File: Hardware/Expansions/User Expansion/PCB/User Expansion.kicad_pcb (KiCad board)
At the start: 2 copper layers, 100 x 70 mm, 876 parts, among them J101 10018784-10201TLF, U101 M24C02-FMN

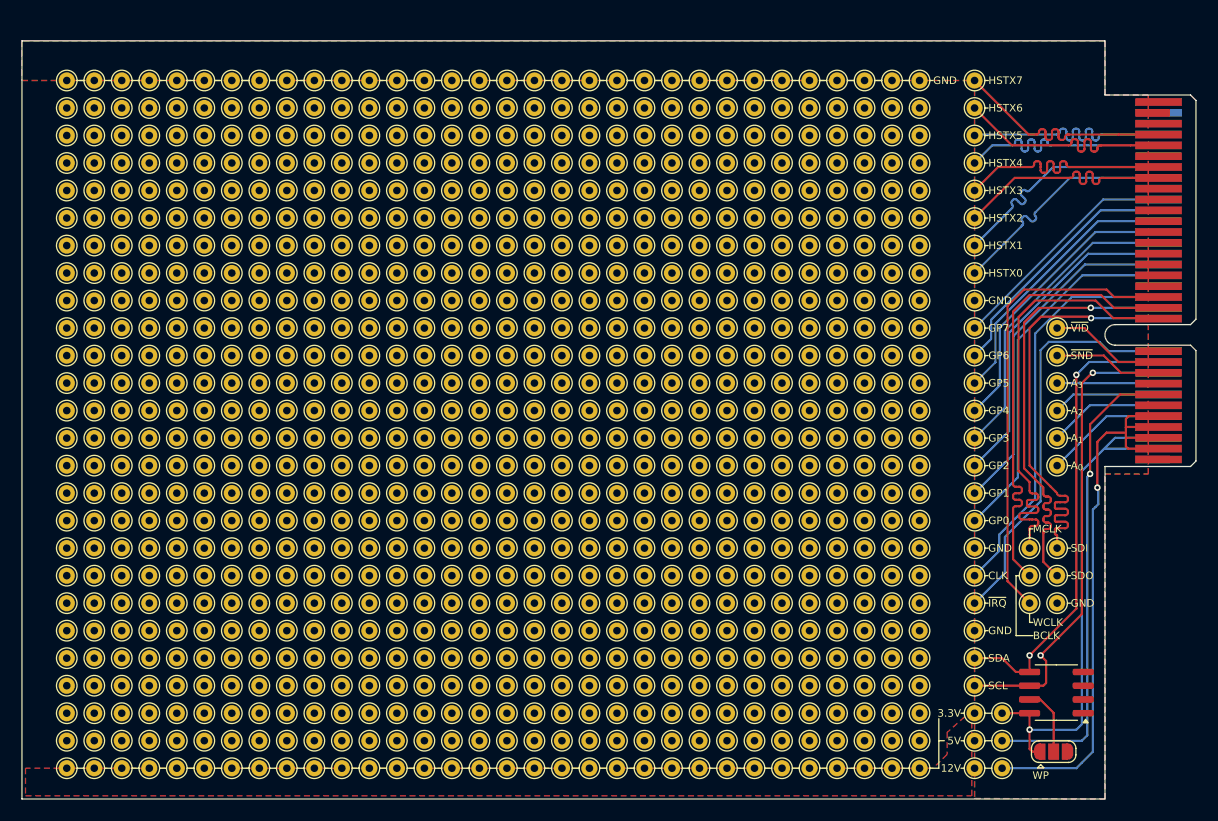
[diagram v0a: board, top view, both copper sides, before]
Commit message: Overhauls user expansion and updates design to new platform decisions.
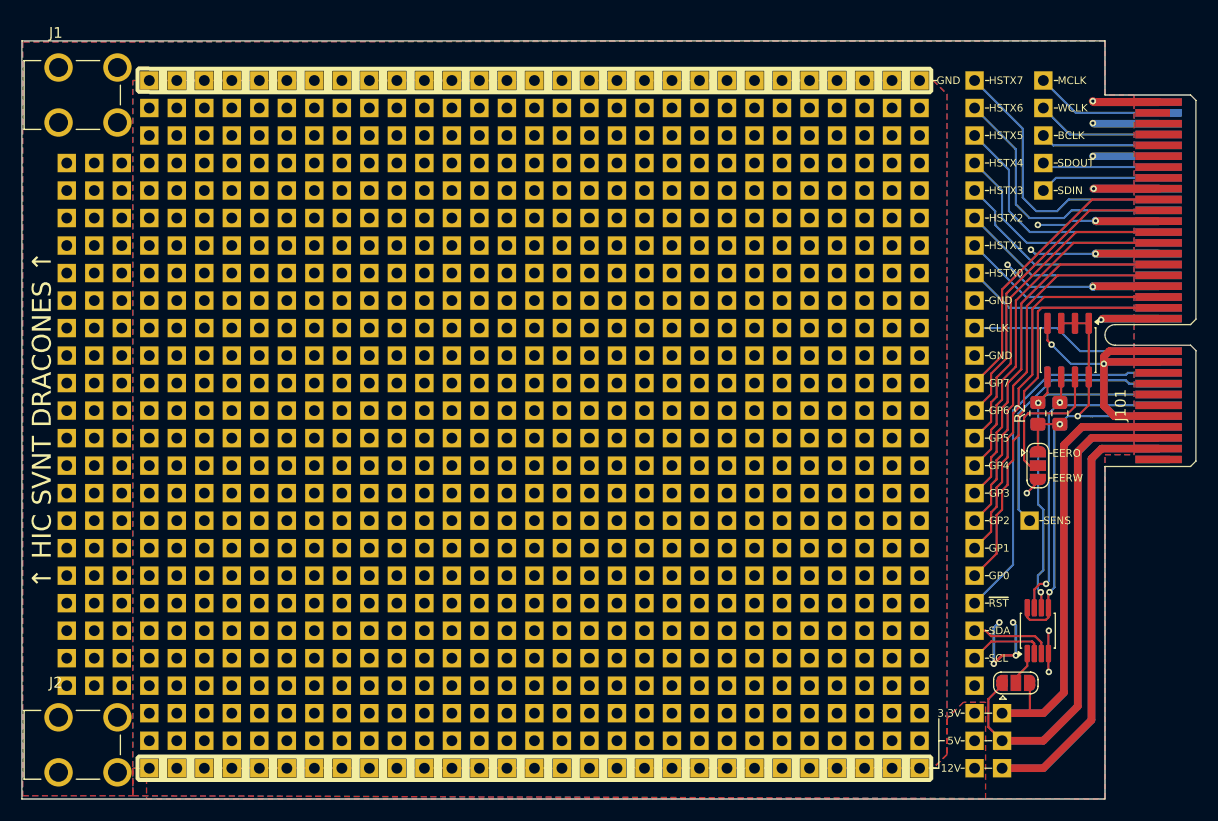
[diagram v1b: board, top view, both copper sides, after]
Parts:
- removed TP1001, TP1002, TP1003, TP1004, TP1005, TP1006, TP1007, TP1008, TP1009, TP1010, TP1011, TP1012, TP1013, TP1014, TP1015, TP1016, TP1017, TP1018, TP1019, TP1020, TP1021, TP1022, TP1023, TP1024, TP1025, TP1026, TP1027, TP1028, TP1029, TP1030, TP1031, TP1032, TP1033, TP1034, TP1035, TP1036, TP1037, TP1038, TP1039, TP1040, TP1041, TP1042, TP1043, TP1044, TP1045, TP1046, TP1047, TP1048, TP1049, TP1050, TP1051, TP1052, TP1053, TP1054, TP1055, TP1056, TP1057, TP1058, TP1059, TP1060, TP1061, TP1062, TP1063, TP1064, TP1101, TP1102, TP1103, TP1104, TP1105, TP1106, TP1107, TP1108, TP1109, TP1110, TP1111, TP1112, TP1113, TP1114, TP1115, TP1116, TP1117, TP1118, TP1119, TP1120, TP1121, TP1122, TP1123, TP1124, TP1125, TP1126, TP1127, TP1128, TP1129, TP1130, TP1131, TP1132, TP1133, TP1134, TP1135, TP1136, TP1137, TP1138, TP1139, TP1140, TP1141, TP1142, TP1143, TP1144, TP1145, TP1146, TP1147, TP1148, TP1149, TP1150, TP1151, TP1152, TP1153, TP1154, TP1155, TP1156, TP1157, TP1158, TP1159, TP1160, TP1161, TP1162, TP1163, TP1164, TP1201, TP1202, TP1203, TP1204, TP1205, TP1206, TP1207, TP1208, TP1209, TP1210, TP1211, TP1212, TP1213, TP1214, TP1215, TP1216, TP1217, TP1218, TP1219, TP1220, TP1221, TP1222, TP1223, TP1224, TP1225, TP1226, TP1227, TP1228, TP1229, TP1230, TP1231, TP1232, TP1233, TP1234, TP1235, TP1236, TP1237, TP1238, TP1239, TP1240, TP1241, TP1242, TP1243, TP1244, TP1245, TP1246, TP1247, TP1248, TP1249, TP1250, TP1251, TP1252, TP1253, TP1254, TP1255, TP1256, TP1257, TP1258, TP1259, TP1260, TP1261, TP1262, TP1263, TP1264, TP1330 (x2), TP1331 (x2), TP1332 (x2), TP1333, TP1334, TP1335, TP1336, TP1337, TP1338, TP1339, TP1340, TP1341, TP1342, TP1343, TP1344, TP1345, TP1346, TP1347, TP1348, TP1349, TP1350, TP1351, TP1352, TP1353, TP1354, TP1355, TP1356, TP1357, TP1358, TP1359, TP1360, TP1361, TP1362, TP1363, TP1364, TP1424, TP1428, TP1432, TP201, TP202, TP203, TP204, TP205, TP206, TP207, TP208, TP209, TP210, TP211, TP212, TP213, TP214, TP215, TP216, TP217, TP218, TP219, TP220, TP221, TP222, TP223, TP224, TP225, TP226, TP227, TP228, TP229, TP230, TP231, TP232, TP233, TP234, TP235, TP236, TP237, TP238, TP239, TP240, TP241, TP242, TP243, TP244, TP245, TP246, TP247, TP248, TP249, TP250, TP251, TP252, TP253, TP254, TP255, TP256, TP257, TP258, TP259, TP260, TP261, TP262, TP263, TP264, TP301, TP302, TP303, TP304, TP305, TP306, TP307, TP308, TP309, TP310, TP311, TP312, TP313, TP314, TP315, TP316, TP317, TP318, TP319, TP320, TP321, TP322, TP323, TP324, TP325, TP326, TP327, TP328, TP329, TP330, TP331, TP332, TP333, TP334, TP335, TP336, TP337, TP338, TP339, TP340, TP341, TP342, TP343, TP344, TP345, TP346, TP347, TP348, TP349, TP350, TP351, TP352, TP353, TP354, TP355, TP356, TP357, TP358, TP359, TP360, TP361, TP362, TP363, TP364, TP401, TP402, TP403, TP404, TP405, TP406, TP407, TP408, TP409, TP410, TP411, TP412, TP413, TP414, TP415, TP416, TP417, TP418, TP419, TP420, TP421, TP422, TP423, TP424, TP425, TP426, TP427, TP428, TP429, TP430, TP431, TP432, TP433, TP434, TP435, TP436, TP437, TP438, TP439, TP440, TP441, TP442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: -, TestPoint:TestPoint_THTPad_D1.5mm_Drill0.7mm
- removed TP102: SCL, TestPoint:TestPoint_THTPad_D1.5mm_Drill0.7mm
- removed TP103: SDA, TestPoint:TestPoint_THTPad_D1.5mm_Drill0.7mm
- removed TP128: WCLK, TestPoint:TestPoint_THTPad_D1.5mm_Drill0.7mm
- removed TP129: HSTX2, TestPoint:TestPoint_THTPad_D1.5mm_Drill0.7mm
- removed TP130: HSTX3, TestPoint:TestPoint_THTPad_D1.5mm_Drill0.7mm
- removed the TP1301 at (165.1, 96.5)
- removed the TP1302 at (165.1, 104.1)
- removed the TP1303 at (167.6, 94.0)
- removed the TP1304 at (167.6, 104.1)
- removed the TP1305 at (175.3, 94.0)
- removed the TP1306 at (175.3, 96.5)
- removed the TP1307 at (175.3, 99.1)
- removed the TP1308 at (175.3, 101.6)
- removed the TP1309 at (165.1, 94.0)
- removed TP131: HSTX6, TestPoint:TestPoint_THTPad_D1.5mm_Drill0.7mm
- removed the TP1310 at (165.1, 106.7)
- removed the TP1311 at (167.6, 96.5)
- removed the TP1312 at (167.6, 106.7)
- removed the TP1313 at (175.3, 104.1)
- removed the TP1314 at (175.3, 106.7)
- removed the TP1315 at (175.3, 109.2)
- removed the TP1316 at (175.3, 111.8)
- removed the TP1317 at (165.1, 99.1)
- removed the TP1318 at (165.1, 109.2)
- removed the TP1319 at (167.6, 99.1)
- removed the TP1320 at (167.6, 109.2)
- removed the TP1321 at (177.8, 94.0)
- removed the TP1322 at (177.8, 96.5)
- removed the TP1323 at (177.8, 99.1)
- removed the TP1324 at (177.8, 101.6)
- removed the TP1325 at (165.1, 101.6)
- removed the TP1326 at (165.1, 111.8)
- removed the TP1327 at (167.6, 101.6)
- removed the TP1328 at (167.6, 111.8)
- removed the TP1329 at (177.8, 104.1)
- removed TP134: GP7, TestPoint:TestPoint_THTPad_D1.5mm_Drill0.7mm
- removed U101: M24C02-FMN, Package_SO:SOIC-8_3.9x4.9mm_P1.27mm
- added J1: 7774, Home Computer:KEYSTONE_7774, F.Cu at (106.1, 75.0)
- added J2: 7774, Home Computer:KEYSTONE_7774, F.Cu at (106.1, 135.0)
- added JP102: WP, Jumper:SolderJumper-3_P1.3mm_Open_RoundedPad1.0x1.5mm, F.Cu at (191.8, 129.3)
- added R1: 10K, Resistor_SMD:R_0805_2012Metric_Pad1.20x1.40mm_HandSolder, F.Cu at (195.8, 104.4)
- added R2: 10K, Resistor_SMD:R_0805_2012Metric_Pad1.20x1.40mm_HandSolder, F.Cu at (193.8, 104.4)
- added REF**10: Home Computer:Perfboard_Pad_P2.54mm, Home Computer:Perfboard_Pad_P2.54mm, F.Cu at (129.5, 76.2)
- added REF**100: Home Computer:Perfboard_Pad_P2.54mm, Home Computer:Perfboard_Pad_P2.54mm, F.Cu at (114.3, 83.8)
- added REF**101: Home Computer:Perfboard_Pad_P2.54mm, Home Computer:Perfboard_Pad_P2.54mm, F.Cu at (116.8, 83.8)
- added REF**102: Home Computer:Perfboard_Pad_P2.54mm, Home Computer:Perfboard_Pad_P2.54mm, F.Cu at (119.4, 83.8)
- added REF**103: Home Computer:Perfboard_Pad_P2.54mm, Home Computer:Perfboard_Pad_P2.54mm, F.Cu at (121.9, 83.8)
- added REF**104: Home Computer:Perfboard_Pad_P2.54mm, Home Computer:Perfboard_Pad_P2.54mm, F.Cu at (124.5, 83.8)
- added REF**105: Home Computer:Perfboard_Pad_P2.54mm, Home Computer:Perfboard_Pad_P2.54mm, F.Cu at (127.0, 83.8)
- added REF**106: Home Computer:Perfboard_Pad_P2.54mm, Home Computer:Perfboard_Pad_P2.54mm, F.Cu at (129.5, 83.8)
- added REF**107: Home Computer:Perfboard_Pad_P2.54mm, Home Computer:Perfboard_Pad_P2.54mm, F.Cu at (132.1, 83.8)
- added REF**108: Home Computer:Perfboard_Pad_P2.54mm, Home Computer:Perfboard_Pad_P2.54mm, F.Cu at (134.6, 83.8)
- added REF**109: Home Computer:Perfboard_Pad_P2.54mm, Home Computer:Perfboard_Pad_P2.54mm, F.Cu at (137.2, 83.8)
- added REF**11: Home Computer:Perfboard_Pad_P2.54mm, Home Computer:Perfboard_Pad_P2.54mm, F.Cu at (132.1, 76.2)
- added REF**110: Home Computer:Perfboard_Pad_P2.54mm, Home Computer:Perfboard_Pad_P2.54mm, F.Cu at (139.7, 83.8)
- added REF**111: Home Computer:Perfboard_Pad_P2.54mm, Home Computer:Perfboard_Pad_P2.54mm, F.Cu at (142.2, 83.8)
- added REF**112: Home Computer:Perfboard_Pad_P2.54mm, Home Computer:Perfboard_Pad_P2.54mm, F.Cu at (144.8, 83.8)
- added REF**113: Home Computer:Perfboard_Pad_P2.54mm, Home Computer:Perfboard_Pad_P2.54mm, F.Cu at (147.3, 83.8)
- added REF**114: Home Computer:Perfboard_Pad_P2.54mm, Home Computer:Perfboard_Pad_P2.54mm, F.Cu at (149.9, 83.8)
- added REF**115: Home Computer:Perfboard_Pad_P2.54mm, Home Computer:Perfboard_Pad_P2.54mm, F.Cu at (152.4, 83.8)
- added REF**116: Home Computer:Perfboard_Pad_P2.54mm, Home Computer:Perfboard_Pad_P2.54mm, F.Cu at (154.9, 83.8)
- added REF**117: Home Computer:Perfboard_Pad_P2.54mm, Home Computer:Perfboard_Pad_P2.54mm, F.Cu at (157.5, 83.8)
- added REF**118: Home Computer:Perfboard_Pad_P2.54mm, Home Computer:Perfboard_Pad_P2.54mm, F.Cu at (160.0, 83.8)
- added REF**119: Home Computer:Perfboard_Pad_P2.54mm, Home Computer:Perfboard_Pad_P2.54mm, F.Cu at (162.6, 83.8)
- added REF**12: Home Computer:Perfboard_Pad_P2.54mm, Home Computer:Perfboard_Pad_P2.54mm, F.Cu at (134.6, 76.2)
- added REF**120: Home Computer:Perfboard_Pad_P2.54mm, Home Computer:Perfboard_Pad_P2.54mm, F.Cu at (165.1, 83.8)
- added REF**121: Home Computer:Perfboard_Pad_P2.54mm, Home Computer:Perfboard_Pad_P2.54mm, F.Cu at (167.6, 83.8)
- added REF**122: Home Computer:Perfboard_Pad_P2.54mm, Home Computer:Perfboard_Pad_P2.54mm, F.Cu at (170.2, 83.8)
- added REF**123: Home Computer:Perfboard_Pad_P2.54mm, Home Computer:Perfboard_Pad_P2.54mm, F.Cu at (172.7, 83.8)
- added REF**124: Home Computer:Perfboard_Pad_P2.54mm, Home Computer:Perfboard_Pad_P2.54mm, F.Cu at (175.3, 83.8)
- added REF**125: Home Computer:Perfboard_Pad_P2.54mm, Home Computer:Perfboard_Pad_P2.54mm, F.Cu at (177.8, 83.8)
- added REF**126: Home Computer:Perfboard_Pad_P2.54mm, Home Computer:Perfboard_Pad_P2.54mm, F.Cu at (180.3, 83.8)
- added REF**127: Home Computer:Perfboard_Pad_P2.54mm, Home Computer:Perfboard_Pad_P2.54mm, F.Cu at (182.9, 83.8)
- added REF**128: Home Computer:Perfboard_Pad_P2.54mm, Home Computer:Perfboard_Pad_P2.54mm, F.Cu at (104.1, 86.4)
- added REF**129: Home Computer:Perfboard_Pad_P2.54mm, Home Computer:Perfboard_Pad_P2.54mm, F.Cu at (106.7, 86.4)
- added REF**13: Home Computer:Perfboard_Pad_P2.54mm, Home Computer:Perfboard_Pad_P2.54mm, F.Cu at (137.2, 76.2)
- added REF**130: Home Computer:Perfboard_Pad_P2.54mm, Home Computer:Perfboard_Pad_P2.54mm, F.Cu at (109.2, 86.4)
- added REF**131: Home Computer:Perfboard_Pad_P2.54mm, Home Computer:Perfboard_Pad_P2.54mm, F.Cu at (111.8, 86.4)
- added REF**132: Home Computer:Perfboard_Pad_P2.54mm, Home Computer:Perfboard_Pad_P2.54mm, F.Cu at (114.3, 86.4)
- added REF**133: Home Computer:Perfboard_Pad_P2.54mm, Home Computer:Perfboard_Pad_P2.54mm, F.Cu at (116.8, 86.4)
- added REF**134: Home Computer:Perfboard_Pad_P2.54mm, Home Computer:Perfboard_Pad_P2.54mm, F.Cu at (119.4, 86.4)
- added REF**135: Home Computer:Perfboard_Pad_P2.54mm, Home Computer:Perfboard_Pad_P2.54mm, F.Cu at (121.9, 86.4)
- added REF**136: Home Computer:Perfboard_Pad_P2.54mm, Home Computer:Perfboard_Pad_P2.54mm, F.Cu at (124.5, 86.4)
- added REF**137: Home Computer:Perfboard_Pad_P2.54mm, Home Computer:Perfboard_Pad_P2.54mm, F.Cu at (127.0, 86.4)
- added REF**138: Home Computer:Perfboard_Pad_P2.54mm, Home Computer:Perfboard_Pad_P2.54mm, F.Cu at (129.5, 86.4)
- added REF**139: Home Computer:Perfboard_Pad_P2.54mm, Home Computer:Perfboard_Pad_P2.54mm, F.Cu at (132.1, 86.4)
- added REF**14: Home Computer:Perfboard_Pad_P2.54mm, Home Computer:Perfboard_Pad_P2.54mm, F.Cu at (139.7, 76.2)
- added REF**140: Home Computer:Perfboard_Pad_P2.54mm, Home Computer:Perfboard_Pad_P2.54mm, F.Cu at (134.6, 86.4)
- added REF**141: Home Computer:Perfboard_Pad_P2.54mm, Home Computer:Perfboard_Pad_P2.54mm, F.Cu at (137.2, 86.4)
- added REF**142: Home Computer:Perfboard_Pad_P2.54mm, Home Computer:Perfboard_Pad_P2.54mm, F.Cu at (139.7, 86.4)
- added REF**143: Home Computer:Perfboard_Pad_P2.54mm, Home Computer:Perfboard_Pad_P2.54mm, F.Cu at (142.2, 86.4)
- added REF**144: Home Computer:Perfboard_Pad_P2.54mm, Home Computer:Perfboard_Pad_P2.54mm, F.Cu at (144.8, 86.4)
- added REF**145: Home Computer:Perfboard_Pad_P2.54mm, Home Computer:Perfboard_Pad_P2.54mm, F.Cu at (147.3, 86.4)
- added REF**146: Home Computer:Perfboard_Pad_P2.54mm, Home Computer:Perfboard_Pad_P2.54mm, F.Cu at (149.9, 86.4)
- added REF**147: Home Computer:Perfboard_Pad_P2.54mm, Home Computer:Perfboard_Pad_P2.54mm, F.Cu at (152.4, 86.4)
- added REF**148: Home Computer:Perfboard_Pad_P2.54mm, Home Computer:Perfboard_Pad_P2.54mm, F.Cu at (154.9, 86.4)
- added REF**149: Home Computer:Perfboard_Pad_P2.54mm, Home Computer:Perfboard_Pad_P2.54mm, F.Cu at (157.5, 86.4)
- added REF**15: Home Computer:Perfboard_Pad_P2.54mm, Home Computer:Perfboard_Pad_P2.54mm, F.Cu at (142.2, 76.2)
- added REF**150: Home Computer:Perfboard_Pad_P2.54mm, Home Computer:Perfboard_Pad_P2.54mm, F.Cu at (160.0, 86.4)
- added REF**151: Home Computer:Perfboard_Pad_P2.54mm, Home Computer:Perfboard_Pad_P2.54mm, F.Cu at (162.6, 86.4)
- added REF**152: Home Computer:Perfboard_Pad_P2.54mm, Home Computer:Perfboard_Pad_P2.54mm, F.Cu at (165.1, 86.4)
- added REF**153: Home Computer:Perfboard_Pad_P2.54mm, Home Computer:Perfboard_Pad_P2.54mm, F.Cu at (167.6, 86.4)
- added REF**154: Home Computer:Perfboard_Pad_P2.54mm, Home Computer:Perfboard_Pad_P2.54mm, F.Cu at (170.2, 86.4)
- added REF**155: Home Computer:Perfboard_Pad_P2.54mm, Home Computer:Perfboard_Pad_P2.54mm, F.Cu at (172.7, 86.4)
- added REF**156: Home Computer:Perfboard_Pad_P2.54mm, Home Computer:Perfboard_Pad_P2.54mm, F.Cu at (175.3, 86.4)
- added REF**157: Home Computer:Perfboard_Pad_P2.54mm, Home Computer:Perfboard_Pad_P2.54mm, F.Cu at (177.8, 86.4)
- added REF**158: Home Computer:Perfboard_Pad_P2.54mm, Home Computer:Perfboard_Pad_P2.54mm, F.Cu at (180.3, 86.4)
- added REF**159: Home Computer:Perfboard_Pad_P2.54mm, Home Computer:Perfboard_Pad_P2.54mm, F.Cu at (182.9, 86.4)
- added REF**16: Home Computer:Perfboard_Pad_P2.54mm, Home Computer:Perfboard_Pad_P2.54mm, F.Cu at (144.8, 76.2)
- added REF**160: Home Computer:Perfboard_Pad_P2.54mm, Home Computer:Perfboard_Pad_P2.54mm, F.Cu at (104.1, 88.9)
- added REF**161: Home Computer:Perfboard_Pad_P2.54mm, Home Computer:Perfboard_Pad_P2.54mm, F.Cu at (106.7, 88.9)
- added REF**162: Home Computer:Perfboard_Pad_P2.54mm, Home Computer:Perfboard_Pad_P2.54mm, F.Cu at (109.2, 88.9)
- added REF**163: Home Computer:Perfboard_Pad_P2.54mm, Home Computer:Perfboard_Pad_P2.54mm, F.Cu at (111.8, 88.9)
- added REF**164: Home Computer:Perfboard_Pad_P2.54mm, Home Computer:Perfboard_Pad_P2.54mm, F.Cu at (114.3, 88.9)
- added REF**165: Home Computer:Perfboard_Pad_P2.54mm, Home Computer:Perfboard_Pad_P2.54mm, F.Cu at (116.8, 88.9)
- added REF**166: Home Computer:Perfboard_Pad_P2.54mm, Home Computer:Perfboard_Pad_P2.54mm, F.Cu at (119.4, 88.9)
- added REF**167: Home Computer:Perfboard_Pad_P2.54mm, Home Computer:Perfboard_Pad_P2.54mm, F.Cu at (121.9, 88.9)
- added REF**168: Home Computer:Perfboard_Pad_P2.54mm, Home Computer:Perfboard_Pad_P2.54mm, F.Cu at (124.5, 88.9)
- added REF**169: Home Computer:Perfboard_Pad_P2.54mm, Home Computer:Perfboard_Pad_P2.54mm, F.Cu at (127.0, 88.9)
- added REF**17: Home Computer:Perfboard_Pad_P2.54mm, Home Computer:Perfboard_Pad_P2.54mm, F.Cu at (147.3, 76.2)
- added REF**170: Home Computer:Perfboard_Pad_P2.54mm, Home Computer:Perfboard_Pad_P2.54mm, F.Cu at (129.5, 88.9)
- added REF**171: Home Computer:Perfboard_Pad_P2.54mm, Home Computer:Perfboard_Pad_P2.54mm, F.Cu at (132.1, 88.9)
- added REF**172: Home Computer:Perfboard_Pad_P2.54mm, Home Computer:Perfboard_Pad_P2.54mm, F.Cu at (134.6, 88.9)
- added REF**173: Home Computer:Perfboard_Pad_P2.54mm, Home Computer:Perfboard_Pad_P2.54mm, F.Cu at (137.2, 88.9)
- added REF**174: Home Computer:Perfboard_Pad_P2.54mm, Home Computer:Perfboard_Pad_P2.54mm, F.Cu at (139.7, 88.9)
- added REF**175: Home Computer:Perfboard_Pad_P2.54mm, Home Computer:Perfboard_Pad_P2.54mm, F.Cu at (142.2, 88.9)
- added REF**176: Home Computer:Perfboard_Pad_P2.54mm, Home Computer:Perfboard_Pad_P2.54mm, F.Cu at (144.8, 88.9)
- added REF**177: Home Computer:Perfboard_Pad_P2.54mm, Home Computer:Perfboard_Pad_P2.54mm, F.Cu at (147.3, 88.9)
- added REF**178: Home Computer:Perfboard_Pad_P2.54mm, Home Computer:Perfboard_Pad_P2.54mm, F.Cu at (149.9, 88.9)
- added REF**179: Home Computer:Perfboard_Pad_P2.54mm, Home Computer:Perfboard_Pad_P2.54mm, F.Cu at (152.4, 88.9)
- added REF**18: Home Computer:Perfboard_Pad_P2.54mm, Home Computer:Perfboard_Pad_P2.54mm, F.Cu at (149.9, 76.2)
- added REF**180: Home Computer:Perfboard_Pad_P2.54mm, Home Computer:Perfboard_Pad_P2.54mm, F.Cu at (154.9, 88.9)
- added REF**181: Home Computer:Perfboard_Pad_P2.54mm, Home Computer:Perfboard_Pad_P2.54mm, F.Cu at (157.5, 88.9)
- added REF**182: Home Computer:Perfboard_Pad_P2.54mm, Home Computer:Perfboard_Pad_P2.54mm, F.Cu at (160.0, 88.9)
- added REF**183: Home Computer:Perfboard_Pad_P2.54mm, Home Computer:Perfboard_Pad_P2.54mm, F.Cu at (162.6, 88.9)
- added REF**184: Home Computer:Perfboard_Pad_P2.54mm, Home Computer:Perfboard_Pad_P2.54mm, F.Cu at (165.1, 88.9)
- added REF**185: Home Computer:Perfboard_Pad_P2.54mm, Home Computer:Perfboard_Pad_P2.54mm, F.Cu at (167.6, 88.9)
- added REF**186: Home Computer:Perfboard_Pad_P2.54mm, Home Computer:Perfboard_Pad_P2.54mm, F.Cu at (170.2, 88.9)
- added REF**187: Home Computer:Perfboard_Pad_P2.54mm, Home Computer:Perfboard_Pad_P2.54mm, F.Cu at (172.7, 88.9)
- added REF**188: Home Computer:Perfboard_Pad_P2.54mm, Home Computer:Perfboard_Pad_P2.54mm, F.Cu at (175.3, 88.9)
- added REF**189: Home Computer:Perfboard_Pad_P2.54mm, Home Computer:Perfboard_Pad_P2.54mm, F.Cu at (177.8, 88.9)
- added REF**19: Home Computer:Perfboard_Pad_P2.54mm, Home Computer:Perfboard_Pad_P2.54mm, F.Cu at (152.4, 76.2)
- added REF**190: Home Computer:Perfboard_Pad_P2.54mm, Home Computer:Perfboard_Pad_P2.54mm, F.Cu at (180.3, 88.9)
- added REF**191: Home Computer:Perfboard_Pad_P2.54mm, Home Computer:Perfboard_Pad_P2.54mm, F.Cu at (182.9, 88.9)
- added REF**192: Home Computer:Perfboard_Pad_P2.54mm, Home Computer:Perfboard_Pad_P2.54mm, F.Cu at (104.1, 91.4)
- added REF**193: Home Computer:Perfboard_Pad_P2.54mm, Home Computer:Perfboard_Pad_P2.54mm, F.Cu at (106.7, 91.4)
- added REF**194: Home Computer:Perfboard_Pad_P2.54mm, Home Computer:Perfboard_Pad_P2.54mm, F.Cu at (109.2, 91.4)
- added REF**195: Home Computer:Perfboard_Pad_P2.54mm, Home Computer:Perfboard_Pad_P2.54mm, F.Cu at (111.8, 91.4)
- added REF**196: Home Computer:Perfboard_Pad_P2.54mm, Home Computer:Perfboard_Pad_P2.54mm, F.Cu at (114.3, 91.4)
- added REF**197: Home Computer:Perfboard_Pad_P2.54mm, Home Computer:Perfboard_Pad_P2.54mm, F.Cu at (116.8, 91.4)
- added REF**198: Home Computer:Perfboard_Pad_P2.54mm, Home Computer:Perfboard_Pad_P2.54mm, F.Cu at (119.4, 91.4)
- added REF**199: Home Computer:Perfboard_Pad_P2.54mm, Home Computer:Perfboard_Pad_P2.54mm, F.Cu at (121.9, 91.4)
- added REF**20: Home Computer:Perfboard_Pad_P2.54mm, Home Computer:Perfboard_Pad_P2.54mm, F.Cu at (154.9, 76.2)
- added REF**200: Home Computer:Perfboard_Pad_P2.54mm, Home Computer:Perfboard_Pad_P2.54mm, F.Cu at (124.5, 91.4)
- added REF**201: Home Computer:Perfboard_Pad_P2.54mm, Home Computer:Perfboard_Pad_P2.54mm, F.Cu at (127.0, 91.4)
- added REF**202: Home Computer:Perfboard_Pad_P2.54mm, Home Computer:Perfboard_Pad_P2.54mm, F.Cu at (129.5, 91.4)
- added REF**203: Home Computer:Perfboard_Pad_P2.54mm, Home Computer:Perfboard_Pad_P2.54mm, F.Cu at (132.1, 91.4)
- added REF**204: Home Computer:Perfboard_Pad_P2.54mm, Home Computer:Perfboard_Pad_P2.54mm, F.Cu at (134.6, 91.4)
- added REF**205: Home Computer:Perfboard_Pad_P2.54mm, Home Computer:Perfboard_Pad_P2.54mm, F.Cu at (137.2, 91.4)
- added REF**206: Home Computer:Perfboard_Pad_P2.54mm, Home Computer:Perfboard_Pad_P2.54mm, F.Cu at (139.7, 91.4)
- added REF**207: Home Computer:Perfboard_Pad_P2.54mm, Home Computer:Perfboard_Pad_P2.54mm, F.Cu at (142.2, 91.4)
- added REF**208: Home Computer:Perfboard_Pad_P2.54mm, Home Computer:Perfboard_Pad_P2.54mm, F.Cu at (144.8, 91.4)
- added REF**209: Home Computer:Perfboard_Pad_P2.54mm, Home Computer:Perfboard_Pad_P2.54mm, F.Cu at (147.3, 91.4)
- added REF**21: Home Computer:Perfboard_Pad_P2.54mm, Home Computer:Perfboard_Pad_P2.54mm, F.Cu at (157.5, 76.2)
- added REF**210: Home Computer:Perfboard_Pad_P2.54mm, Home Computer:Perfboard_Pad_P2.54mm, F.Cu at (149.9, 91.4)
- added REF**211: Home Computer:Perfboard_Pad_P2.54mm, Home Computer:Perfboard_Pad_P2.54mm, F.Cu at (152.4, 91.4)
- added REF**212: Home Computer:Perfboard_Pad_P2.54mm, Home Computer:Perfboard_Pad_P2.54mm, F.Cu at (154.9, 91.4)
- added REF**213: Home Computer:Perfboard_Pad_P2.54mm, Home Computer:Perfboard_Pad_P2.54mm, F.Cu at (157.5, 91.4)
- added REF**214: Home Computer:Perfboard_Pad_P2.54mm, Home Computer:Perfboard_Pad_P2.54mm, F.Cu at (160.0, 91.4)
- added REF**215: Home Computer:Perfboard_Pad_P2.54mm, Home Computer:Perfboard_Pad_P2.54mm, F.Cu at (162.6, 91.4)
- added REF**216: Home Computer:Perfboard_Pad_P2.54mm, Home Computer:Perfboard_Pad_P2.54mm, F.Cu at (165.1, 91.4)
- added REF**217: Home Computer:Perfboard_Pad_P2.54mm, Home Computer:Perfboard_Pad_P2.54mm, F.Cu at (167.6, 91.4)
- added REF**218: Home Computer:Perfboard_Pad_P2.54mm, Home Computer:Perfboard_Pad_P2.54mm, F.Cu at (170.2, 91.4)
- added REF**219: Home Computer:Perfboard_Pad_P2.54mm, Home Computer:Perfboard_Pad_P2.54mm, F.Cu at (172.7, 91.4)
- added REF**22: Home Computer:Perfboard_Pad_P2.54mm, Home Computer:Perfboard_Pad_P2.54mm, F.Cu at (160.0, 76.2)
- added REF**220: Home Computer:Perfboard_Pad_P2.54mm, Home Computer:Perfboard_Pad_P2.54mm, F.Cu at (175.3, 91.4)
- added REF**221: Home Computer:Perfboard_Pad_P2.54mm, Home Computer:Perfboard_Pad_P2.54mm, F.Cu at (177.8, 91.4)
- added REF**222: Home Computer:Perfboard_Pad_P2.54mm, Home Computer:Perfboard_Pad_P2.54mm, F.Cu at (180.3, 91.4)
- added REF**223: Home Computer:Perfboard_Pad_P2.54mm, Home Computer:Perfboard_Pad_P2.54mm, F.Cu at (182.9, 91.4)
- added REF**224: Home Computer:Perfboard_Pad_P2.54mm, Home Computer:Perfboard_Pad_P2.54mm, F.Cu at (104.1, 94.0)
- added REF**225: Home Computer:Perfboard_Pad_P2.54mm, Home Computer:Perfboard_Pad_P2.54mm, F.Cu at (106.7, 94.0)
- added REF**226: Home Computer:Perfboard_Pad_P2.54mm, Home Computer:Perfboard_Pad_P2.54mm, F.Cu at (109.2, 94.0)
- added REF**227: Home Computer:Perfboard_Pad_P2.54mm, Home Computer:Perfboard_Pad_P2.54mm, F.Cu at (111.8, 94.0)
- added REF**228: Home Computer:Perfboard_Pad_P2.54mm, Home Computer:Perfboard_Pad_P2.54mm, F.Cu at (114.3, 94.0)
- added REF**229: Home Computer:Perfboard_Pad_P2.54mm, Home Computer:Perfboard_Pad_P2.54mm, F.Cu at (116.8, 94.0)
- added REF**23: Home Computer:Perfboard_Pad_P2.54mm, Home Computer:Perfboard_Pad_P2.54mm, F.Cu at (162.6, 76.2)
- added REF**230: Home Computer:Perfboard_Pad_P2.54mm, Home Computer:Perfboard_Pad_P2.54mm, F.Cu at (119.4, 94.0)
- added REF**231: Home Computer:Perfboard_Pad_P2.54mm, Home Computer:Perfboard_Pad_P2.54mm, F.Cu at (121.9, 94.0)
- added REF**232: Home Computer:Perfboard_Pad_P2.54mm, Home Computer:Perfboard_Pad_P2.54mm, F.Cu at (124.5, 94.0)
- added REF**233: Home Computer:Perfboard_Pad_P2.54mm, Home Computer:Perfboard_Pad_P2.54mm, F.Cu at (127.0, 94.0)
- added REF**234: Home Computer:Perfboard_Pad_P2.54mm, Home Computer:Perfboard_Pad_P2.54mm, F.Cu at (129.5, 94.0)
- added REF**235: Home Computer:Perfboard_Pad_P2.54mm, Home Computer:Perfboard_Pad_P2.54mm, F.Cu at (132.1, 94.0)
- added REF**236: Home Computer:Perfboard_Pad_P2.54mm, Home Computer:Perfboard_Pad_P2.54mm, F.Cu at (134.6, 94.0)
- added REF**237: Home Computer:Perfboard_Pad_P2.54mm, Home Computer:Perfboard_Pad_P2.54mm, F.Cu at (137.2, 94.0)
- added REF**238: Home Computer:Perfboard_Pad_P2.54mm, Home Computer:Perfboard_Pad_P2.54mm, F.Cu at (139.7, 94.0)
- added REF**239: Home Computer:Perfboard_Pad_P2.54mm, Home Computer:Perfboard_Pad_P2.54mm, F.Cu at (142.2, 94.0)
- added REF**24: Home Computer:Perfboard_Pad_P2.54mm, Home Computer:Perfboard_Pad_P2.54mm, F.Cu at (165.1, 76.2)
- added REF**240: Home Computer:Perfboard_Pad_P2.54mm, Home Computer:Perfboard_Pad_P2.54mm, F.Cu at (144.8, 94.0)
- added REF**241: Home Computer:Perfboard_Pad_P2.54mm, Home Computer:Perfboard_Pad_P2.54mm, F.Cu at (147.3, 94.0)
- added REF**242: Home Computer:Perfboard_Pad_P2.54mm, Home Computer:Perfboard_Pad_P2.54mm, F.Cu at (149.9, 94.0)
- added REF**243: Home Computer:Perfboard_Pad_P2.54mm, Home Computer:Perfboard_Pad_P2.54mm, F.Cu at (152.4, 94.0)
- added REF**244: Home Computer:Perfboard_Pad_P2.54mm, Home Computer:Perfboard_Pad_P2.54mm, F.Cu at (154.9, 94.0)
- added REF**245: Home Computer:Perfboard_Pad_P2.54mm, Home Computer:Perfboard_Pad_P2.54mm, F.Cu at (157.5, 94.0)
- added REF**246: Home Computer:Perfboard_Pad_P2.54mm, Home Computer:Perfboard_Pad_P2.54mm, F.Cu at (160.0, 94.0)
- added REF**247: Home Computer:Perfboard_Pad_P2.54mm, Home Computer:Perfboard_Pad_P2.54mm, F.Cu at (162.6, 94.0)
- added REF**248: Home Computer:Perfboard_Pad_P2.54mm, Home Computer:Perfboard_Pad_P2.54mm, F.Cu at (165.1, 94.0)
- added REF**249: Home Computer:Perfboard_Pad_P2.54mm, Home Computer:Perfboard_Pad_P2.54mm, F.Cu at (167.6, 94.0)
- added REF**25: Home Computer:Perfboard_Pad_P2.54mm, Home Computer:Perfboard_Pad_P2.54mm, F.Cu at (167.6, 76.2)
- added REF**250: Home Computer:Perfboard_Pad_P2.54mm, Home Computer:Perfboard_Pad_P2.54mm, F.Cu at (170.2, 94.0)
- added REF**251: Home Computer:Perfboard_Pad_P2.54mm, Home Computer:Perfboard_Pad_P2.54mm, F.Cu at (172.7, 94.0)
- added REF**252: Home Computer:Perfboard_Pad_P2.54mm, Home Computer:Perfboard_Pad_P2.54mm, F.Cu at (175.3, 94.0)
- added REF**253: Home Computer:Perfboard_Pad_P2.54mm, Home Computer:Perfboard_Pad_P2.54mm, F.Cu at (177.8, 94.0)
- added REF**254: Home Computer:Perfboard_Pad_P2.54mm, Home Computer:Perfboard_Pad_P2.54mm, F.Cu at (180.3, 94.0)
- added REF**255: Home Computer:Perfboard_Pad_P2.54mm, Home Computer:Perfboard_Pad_P2.54mm, F.Cu at (182.9, 94.0)
- added REF**256: Home Computer:Perfboard_Pad_P2.54mm, Home Computer:Perfboard_Pad_P2.54mm, F.Cu at (104.1, 96.5)
- added REF**257: Home Computer:Perfboard_Pad_P2.54mm, Home Computer:Perfboard_Pad_P2.54mm, F.Cu at (106.7, 96.5)
- added REF**258: Home Computer:Perfboard_Pad_P2.54mm, Home Computer:Perfboard_Pad_P2.54mm, F.Cu at (109.2, 96.5)
- added REF**259: Home Computer:Perfboard_Pad_P2.54mm, Home Computer:Perfboard_Pad_P2.54mm, F.Cu at (111.8, 96.5)
- added REF**26: Home Computer:Perfboard_Pad_P2.54mm, Home Computer:Perfboard_Pad_P2.54mm, F.Cu at (170.2, 76.2)
- added REF**260: Home Computer:Perfboard_Pad_P2.54mm, Home Computer:Perfboard_Pad_P2.54mm, F.Cu at (114.3, 96.5)
- added REF**261: Home Computer:Perfboard_Pad_P2.54mm, Home Computer:Perfboard_Pad_P2.54mm, F.Cu at (116.8, 96.5)
- added REF**262: Home Computer:Perfboard_Pad_P2.54mm, Home Computer:Perfboard_Pad_P2.54mm, F.Cu at (119.4, 96.5)
- added REF**263: Home Computer:Perfboard_Pad_P2.54mm, Home Computer:Perfboard_Pad_P2.54mm, F.Cu at (121.9, 96.5)
- added REF**264: Home Computer:Perfboard_Pad_P2.54mm, Home Computer:Perfboard_Pad_P2.54mm, F.Cu at (124.5, 96.5)
- added REF**265: Home Computer:Perfboard_Pad_P2.54mm, Home Computer:Perfboard_Pad_P2.54mm, F.Cu at (127.0, 96.5)
- added REF**266: Home Computer:Perfboard_Pad_P2.54mm, Home Computer:Perfboard_Pad_P2.54mm, F.Cu at (129.5, 96.5)
- added REF**267: Home Computer:Perfboard_Pad_P2.54mm, Home Computer:Perfboard_Pad_P2.54mm, F.Cu at (132.1, 96.5)
- added REF**268: Home Computer:Perfboard_Pad_P2.54mm, Home Computer:Perfboard_Pad_P2.54mm, F.Cu at (134.6, 96.5)
- added REF**269: Home Computer:Perfboard_Pad_P2.54mm, Home Computer:Perfboard_Pad_P2.54mm, F.Cu at (137.2, 96.5)
- added REF**27: Home Computer:Perfboard_Pad_P2.54mm, Home Computer:Perfboard_Pad_P2.54mm, F.Cu at (172.7, 76.2)
- added REF**270: Home Computer:Perfboard_Pad_P2.54mm, Home Computer:Perfboard_Pad_P2.54mm, F.Cu at (139.7, 96.5)
- added REF**271: Home Computer:Perfboard_Pad_P2.54mm, Home Computer:Perfboard_Pad_P2.54mm, F.Cu at (142.2, 96.5)
- added REF**272: Home Computer:Perfboard_Pad_P2.54mm, Home Computer:Perfboard_Pad_P2.54mm, F.Cu at (144.8, 96.5)
- added REF**273: Home Computer:Perfboard_Pad_P2.54mm, Home Computer:Perfboard_Pad_P2.54mm, F.Cu at (147.3, 96.5)
- added REF**274: Home Computer:Perfboard_Pad_P2.54mm, Home Computer:Perfboard_Pad_P2.54mm, F.Cu at (149.9, 96.5)
- added REF**275: Home Computer:Perfboard_Pad_P2.54mm, Home Computer:Perfboard_Pad_P2.54mm, F.Cu at (152.4, 96.5)
- added REF**276: Home Computer:Perfboard_Pad_P2.54mm, Home Computer:Perfboard_Pad_P2.54mm, F.Cu at (154.9, 96.5)
- added REF**277: Home Computer:Perfboard_Pad_P2.54mm, Home Computer:Perfboard_Pad_P2.54mm, F.Cu at (157.5, 96.5)
- added REF**278: Home Computer:Perfboard_Pad_P2.54mm, Home Computer:Perfboard_Pad_P2.54mm, F.Cu at (160.0, 96.5)
- added REF**279: Home Computer:Perfboard_Pad_P2.54mm, Home Computer:Perfboard_Pad_P2.54mm, F.Cu at (162.6, 96.5)
- added REF**28: Home Computer:Perfboard_Pad_P2.54mm, Home Computer:Perfboard_Pad_P2.54mm, F.Cu at (175.3, 76.2)
- added REF**280: Home Computer:Perfboard_Pad_P2.54mm, Home Computer:Perfboard_Pad_P2.54mm, F.Cu at (165.1, 96.5)
- added REF**281: Home Computer:Perfboard_Pad_P2.54mm, Home Computer:Perfboard_Pad_P2.54mm, F.Cu at (167.6, 96.5)
- added REF**282: Home Computer:Perfboard_Pad_P2.54mm, Home Computer:Perfboard_Pad_P2.54mm, F.Cu at (170.2, 96.5)
- added REF**283: Home Computer:Perfboard_Pad_P2.54mm, Home Computer:Perfboard_Pad_P2.54mm, F.Cu at (172.7, 96.5)
- added REF**284: Home Computer:Perfboard_Pad_P2.54mm, Home Computer:Perfboard_Pad_P2.54mm, F.Cu at (175.3, 96.5)
- added REF**285: Home Computer:Perfboard_Pad_P2.54mm, Home Computer:Perfboard_Pad_P2.54mm, F.Cu at (177.8, 96.5)
- added REF**286: Home Computer:Perfboard_Pad_P2.54mm, Home Computer:Perfboard_Pad_P2.54mm, F.Cu at (180.3, 96.5)
- added REF**287: Home Computer:Perfboard_Pad_P2.54mm, Home Computer:Perfboard_Pad_P2.54mm, F.Cu at (182.9, 96.5)
- added REF**288: Home Computer:Perfboard_Pad_P2.54mm, Home Computer:Perfboard_Pad_P2.54mm, F.Cu at (104.1, 99.1)
- added REF**289: Home Computer:Perfboard_Pad_P2.54mm, Home Computer:Perfboard_Pad_P2.54mm, F.Cu at (106.7, 99.1)
- added REF**29: Home Computer:Perfboard_Pad_P2.54mm, Home Computer:Perfboard_Pad_P2.54mm, F.Cu at (177.8, 76.2)
- added REF**290: Home Computer:Perfboard_Pad_P2.54mm, Home Computer:Perfboard_Pad_P2.54mm, F.Cu at (109.2, 99.1)
- added REF**291: Home Computer:Perfboard_Pad_P2.54mm, Home Computer:Perfboard_Pad_P2.54mm, F.Cu at (111.8, 99.1)
- added REF**292: Home Computer:Perfboard_Pad_P2.54mm, Home Computer:Perfboard_Pad_P2.54mm, F.Cu at (114.3, 99.1)
- added REF**293: Home Computer:Perfboard_Pad_P2.54mm, Home Computer:Perfboard_Pad_P2.54mm, F.Cu at (116.8, 99.1)
- added REF**294: Home Computer:Perfboard_Pad_P2.54mm, Home Computer:Perfboard_Pad_P2.54mm, F.Cu at (119.4, 99.1)
- added REF**295: Home Computer:Perfboard_Pad_P2.54mm, Home Computer:Perfboard_Pad_P2.54mm, F.Cu at (121.9, 99.1)
- added REF**296: Home Computer:Perfboard_Pad_P2.54mm, Home Computer:Perfboard_Pad_P2.54mm, F.Cu at (124.5, 99.1)
- added REF**297: Home Computer:Perfboard_Pad_P2.54mm, Home Computer:Perfboard_Pad_P2.54mm, F.Cu at (127.0, 99.1)
- added REF**298: Home Computer:Perfboard_Pad_P2.54mm, Home Computer:Perfboard_Pad_P2.54mm, F.Cu at (129.5, 99.1)
- added REF**299: Home Computer:Perfboard_Pad_P2.54mm, Home Computer:Perfboard_Pad_P2.54mm, F.Cu at (132.1, 99.1)
- added REF**3: Home Computer:Perfboard_Pad_P2.54mm, Home Computer:Perfboard_Pad_P2.54mm, F.Cu at (111.8, 76.2)
- added REF**30: Home Computer:Perfboard_Pad_P2.54mm, Home Computer:Perfboard_Pad_P2.54mm, F.Cu at (180.3, 76.2)
- added REF**300: Home Computer:Perfboard_Pad_P2.54mm, Home Computer:Perfboard_Pad_P2.54mm, F.Cu at (134.6, 99.1)
- added REF**301: Home Computer:Perfboard_Pad_P2.54mm, Home Computer:Perfboard_Pad_P2.54mm, F.Cu at (137.2, 99.1)
- added REF**302: Home Computer:Perfboard_Pad_P2.54mm, Home Computer:Perfboard_Pad_P2.54mm, F.Cu at (139.7, 99.1)
- added REF**303: Home Computer:Perfboard_Pad_P2.54mm, Home Computer:Perfboard_Pad_P2.54mm, F.Cu at (142.2, 99.1)
- added REF**304: Home Computer:Perfboard_Pad_P2.54mm, Home Computer:Perfboard_Pad_P2.54mm, F.Cu at (144.8, 99.1)
- added REF**305: Home Computer:Perfboard_Pad_P2.54mm, Home Computer:Perfboard_Pad_P2.54mm, F.Cu at (147.3, 99.1)
- added REF**306: Home Computer:Perfboard_Pad_P2.54mm, Home Computer:Perfboard_Pad_P2.54mm, F.Cu at (149.9, 99.1)
- added REF**307: Home Computer:Perfboard_Pad_P2.54mm, Home Computer:Perfboard_Pad_P2.54mm, F.Cu at (152.4, 99.1)
- added REF**308: Home Computer:Perfboard_Pad_P2.54mm, Home Computer:Perfboard_Pad_P2.54mm, F.Cu at (154.9, 99.1)
- added REF**309: Home Computer:Perfboard_Pad_P2.54mm, Home Computer:Perfboard_Pad_P2.54mm, F.Cu at (157.5, 99.1)
- added REF**31: Home Computer:Perfboard_Pad_P2.54mm, Home Computer:Perfboard_Pad_P2.54mm, F.Cu at (182.9, 76.2)
- added REF**310: Home Computer:Perfboard_Pad_P2.54mm, Home Computer:Perfboard_Pad_P2.54mm, F.Cu at (160.0, 99.1)
- added REF**311: Home Computer:Perfboard_Pad_P2.54mm, Home Computer:Perfboard_Pad_P2.54mm, F.Cu at (162.6, 99.1)
- added REF**312: Home Computer:Perfboard_Pad_P2.54mm, Home Computer:Perfboard_Pad_P2.54mm, F.Cu at (165.1, 99.1)
- added REF**313: Home Computer:Perfboard_Pad_P2.54mm, Home Computer:Perfboard_Pad_P2.54mm, F.Cu at (167.6, 99.1)
- added REF**314: Home Computer:Perfboard_Pad_P2.54mm, Home Computer:Perfboard_Pad_P2.54mm, F.Cu at (170.2, 99.1)
- added REF**315: Home Computer:Perfboard_Pad_P2.54mm, Home Computer:Perfboard_Pad_P2.54mm, F.Cu at (172.7, 99.1)
- added REF**316: Home Computer:Perfboard_Pad_P2.54mm, Home Computer:Perfboard_Pad_P2.54mm, F.Cu at (175.3, 99.1)
- added REF**317: Home Computer:Perfboard_Pad_P2.54mm, Home Computer:Perfboard_Pad_P2.54mm, F.Cu at (177.8, 99.1)
- added REF**318: Home Computer:Perfboard_Pad_P2.54mm, Home Computer:Perfboard_Pad_P2.54mm, F.Cu at (180.3, 99.1)
- added REF**319: Home Computer:Perfboard_Pad_P2.54mm, Home Computer:Perfboard_Pad_P2.54mm, F.Cu at (182.9, 99.1)
- added REF**320: Home Computer:Perfboard_Pad_P2.54mm, Home Computer:Perfboard_Pad_P2.54mm, F.Cu at (104.1, 101.6)
- added REF**321: Home Computer:Perfboard_Pad_P2.54mm, Home Computer:Perfboard_Pad_P2.54mm, F.Cu at (106.7, 101.6)
- added REF**322: Home Computer:Perfboard_Pad_P2.54mm, Home Computer:Perfboard_Pad_P2.54mm, F.Cu at (109.2, 101.6)
- added REF**323: Home Computer:Perfboard_Pad_P2.54mm, Home Computer:Perfboard_Pad_P2.54mm, F.Cu at (111.8, 101.6)
- added REF**324: Home Computer:Perfboard_Pad_P2.54mm, Home Computer:Perfboard_Pad_P2.54mm, F.Cu at (114.3, 101.6)
- added REF**325: Home Computer:Perfboard_Pad_P2.54mm, Home Computer:Perfboard_Pad_P2.54mm, F.Cu at (116.8, 101.6)
- added REF**326: Home Computer:Perfboard_Pad_P2.54mm, Home Computer:Perfboard_Pad_P2.54mm, F.Cu at (119.4, 101.6)
- added REF**327: Home Computer:Perfboard_Pad_P2.54mm, Home Computer:Perfboard_Pad_P2.54mm, F.Cu at (121.9, 101.6)
- added REF**328: Home Computer:Perfboard_Pad_P2.54mm, Home Computer:Perfboard_Pad_P2.54mm, F.Cu at (124.5, 101.6)
- added REF**329: Home Computer:Perfboard_Pad_P2.54mm, Home Computer:Perfboard_Pad_P2.54mm, F.Cu at (127.0, 101.6)
- added REF**330: Home Computer:Perfboard_Pad_P2.54mm, Home Computer:Perfboard_Pad_P2.54mm, F.Cu at (129.5, 101.6)
- added REF**331: Home Computer:Perfboard_Pad_P2.54mm, Home Computer:Perfboard_Pad_P2.54mm, F.Cu at (132.1, 101.6)
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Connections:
- J101 pad A1: GND -> unconnected-(J101-GND-PadA1)
- J101 pad A10: /SDA -> GND
- J101 pad A11: Net-(J101-~{IRQ}) -> /CLK
- J101 pad A12: Net-(J101-I²S_{SDIN}) -> GND
- J101 pad A13: Net-(J101-I²S_{SDOUT}) -> /HSTX0
- J101 pad A14: Net-(J101-CLK_{16MHz}) -> /HSTX1
- J101 pad A16: Net-(J101-GP0) -> /HSTX2
- J101 pad A17: Net-(J101-GP1) -> /HSTX3
- J101 pad A18: Net-(J101-GP2) -> GND
- J101 pad A19: Net-(J101-GP3) -> /HSTX4
- J101 pad A2: +3V3 -> +12V
- J101 pad A20: Net-(J101-GP4) -> /HSTX5
- J101 pad A21: Net-(J101-GP5) -> GND
- J101 pad A22: Net-(J101-GP6) -> /HSTX6
- J101 pad A23: Net-(J101-GP7) -> /HSTX7
- J101 pad A25: Net-(J101-HSTX_{0}) -> /I2S_SDIN
- J101 pad A26: Net-(J101-HSTX_{1}) -> /I2S_SDOUT
- J101 pad A28: Net-(J101-HSTX_{4}) -> /I2S_BCLK
- J101 pad A29: Net-(J101-HSTX_{5}) -> /I2S_WCLK
- J101 pad A3: +3V3 -> +5V
- J101 pad A31: GND -> /I2S_MCLK
- J101 pad A4: GND -> +3V3
- J101 pad A5: Net-(J101-SLOT_{A0}) -> +3.3VP
- J101 pad A6: Net-(J101-SLOT_{A1}) -> /SCL_{ID}
- J101 pad A7: Net-(J101-SLOT_{A2}) -> /SDA_{ID}
- J101 pad A8: Net-(J101-SLOT_{A3}) -> /MOD_SENS
- J101 pad A9: /SCL -> /~{RESET}
- J101 pad B1: GND -> unconnected-(J101-GND-PadB1)
- J101 pad B10: Net-(J101-~{SLOT_{VIDEO}}) -> GND
- J101 pad B12: Net-(J101-I²S_{MCLK}) -> GND
- J101 pad B13: Net-(J101-I²S_{BCLK}) -> /GP0
- J101 pad B14: Net-(J101-I²S_{WCLK}) -> /GP1
- J101 pad B16: GND -> /GP2
- J101 pad B17: GND -> /GP3
- J101 pad B19: GND -> /GP4
- J101 pad B20: GND -> /GP5
- J101 pad B22: GND -> /GP6
- J101 pad B23: GND -> /GP7
- J101 pad B25: Net-(J101-HSTX_{2}) -> unconnected-(J101-RESERVED0-PadB25)
- J101 pad B26: Net-(J101-HSTX_{3}) -> unconnected-(J101-RESERVED1-PadB26)
- J101 pad B27: GND -> unconnected-(J101-RESERVED2-PadB27)
- J101 pad B28: Net-(J101-HSTX_{6}) -> unconnected-(J101-RESERVED3-PadB28)
- J101 pad B29: Net-(J101-HSTX_{7}) -> unconnected-(J101-RESERVED4-PadB29)
- J101 pad B3: +12V -> +5V
- J101 pad B30: GND -> unconnected-(J101-RESERVED5-PadB30)
- J101 pad B31: GND -> unconnected-(J101-RESERVED6-PadB31)
- J101 pad B4: +12V -> +3V3
- J101 pad B5: +12V -> GND
- J101 pad B6: +5V -> /~{SLOT_AUDIO}
- J101 pad B7: +5V -> /~{SLOT_HS}
- J101 pad B8: GND -> /~{SLOT_FUNC0}
- J101 pad B9: Net-(J101-~{SLOT_{AUDIO}}) -> /~{SLOT_FUNC1}
- JP101 pad 1: +3V3 -> +3.3VP
- TP104 pad 1: Net-(J101-SLOT_{A0}) -> /MOD_SENS
- TP105 pad 1: Net-(J101-SLOT_{A1}) -> /~{RESET}
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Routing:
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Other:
- board text added: "EERO"
- board text added: "EERW"
- board text added: "SDIN"
- board text added: "SDOUT"
- board text added: "SENS"
- board text added: "~{RST}"
- board text added: "↑ HIC SVNT DRACONES ↑"
- board text removed: "A_{0}"
- board text removed: "A_{1}"
- board text removed: "A_{2}"
- board text removed: "A_{3}"
- board text removed: "SDI"
- board text removed: "SDO"
- board text removed: "WP"
- board text removed: "~{IRQ}"
- board text removed: "~{SND}"
- board text removed: "~{VID}"
